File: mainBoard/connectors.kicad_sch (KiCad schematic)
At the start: 55 parts, among them J10 Conn_01x02, J11 Conn_02x05_Odd_Even, J12 Conn_01x02, J14 Conn_01x06, J17 Conn_01x05, J18 Conn_01x04, J19 Conn_01x14, J8 Conn_01x02, J9 Conn_01x02, Q3 IRLML6244TRPBF, Q4 IRLML6244TRPBF, Q5 IRLML6244TRPBF, Q6 IRLML6244TRPBF, Q8 PMOS, U17 SFH617A-2, U18 USBLC6-4SC6, U21 USBLC6-4SC6, U23 USBLC6-4SC6, U24 USBLC6-2SC6, U26 100, U27 100, U28 100, U29 100, U30 74LVC1T45W6-7, U32 74LVC1T45W6-7

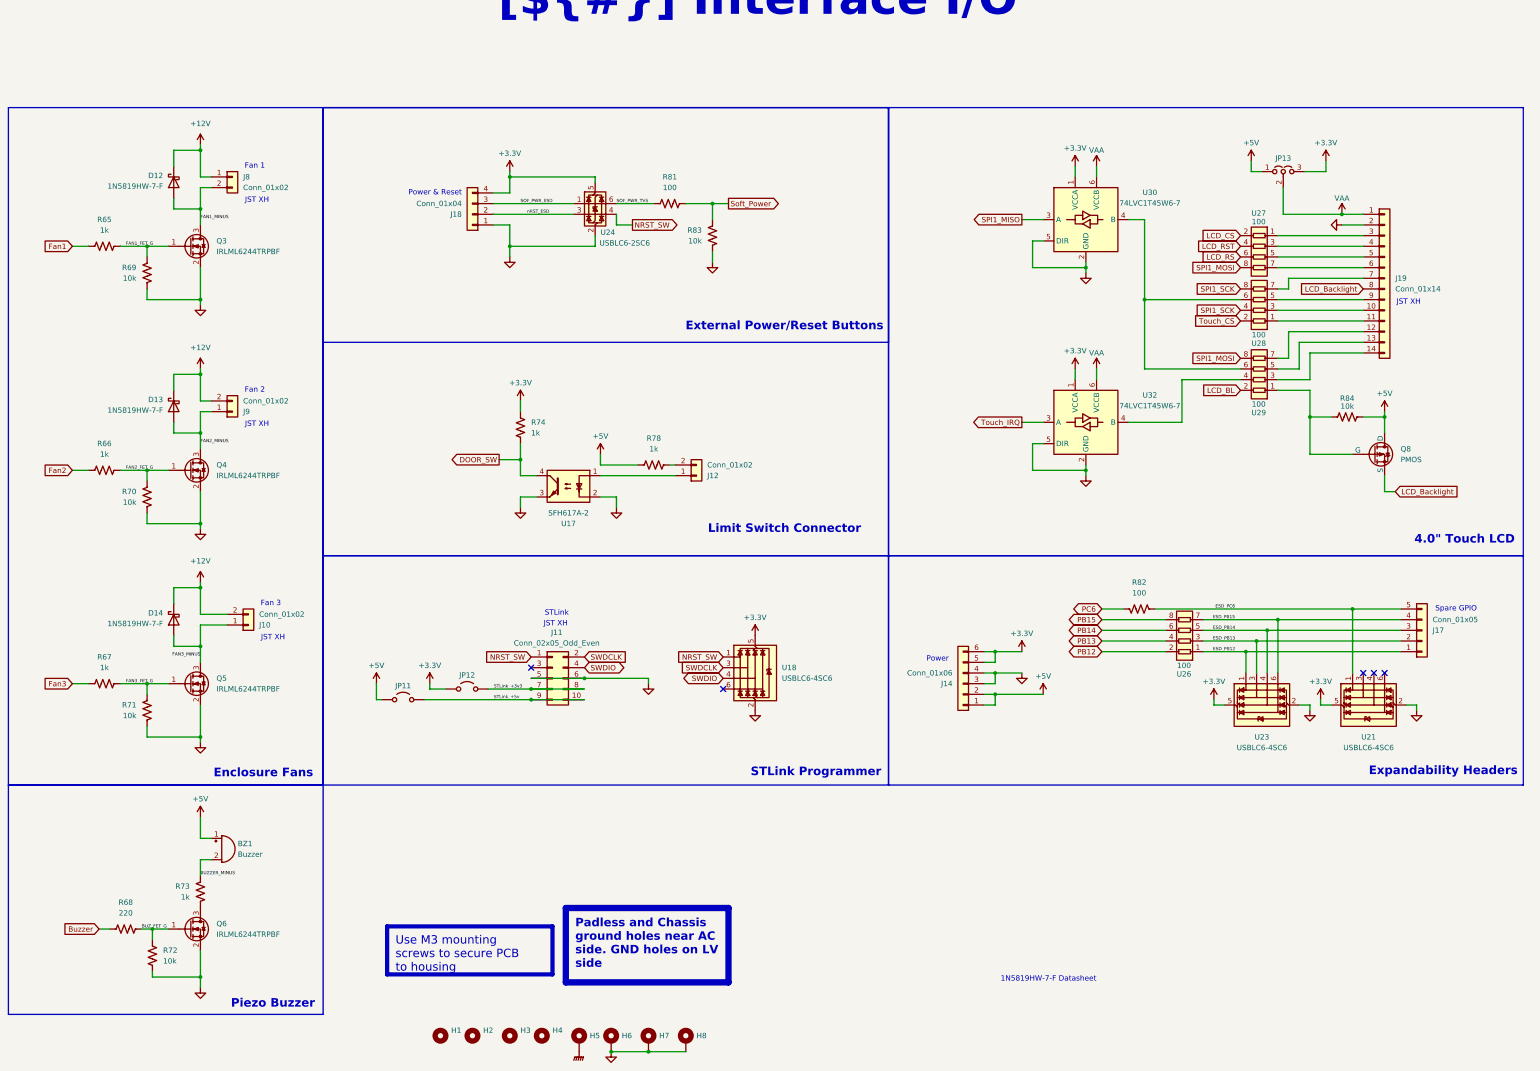
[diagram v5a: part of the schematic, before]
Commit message: replace piezo with actual speaker
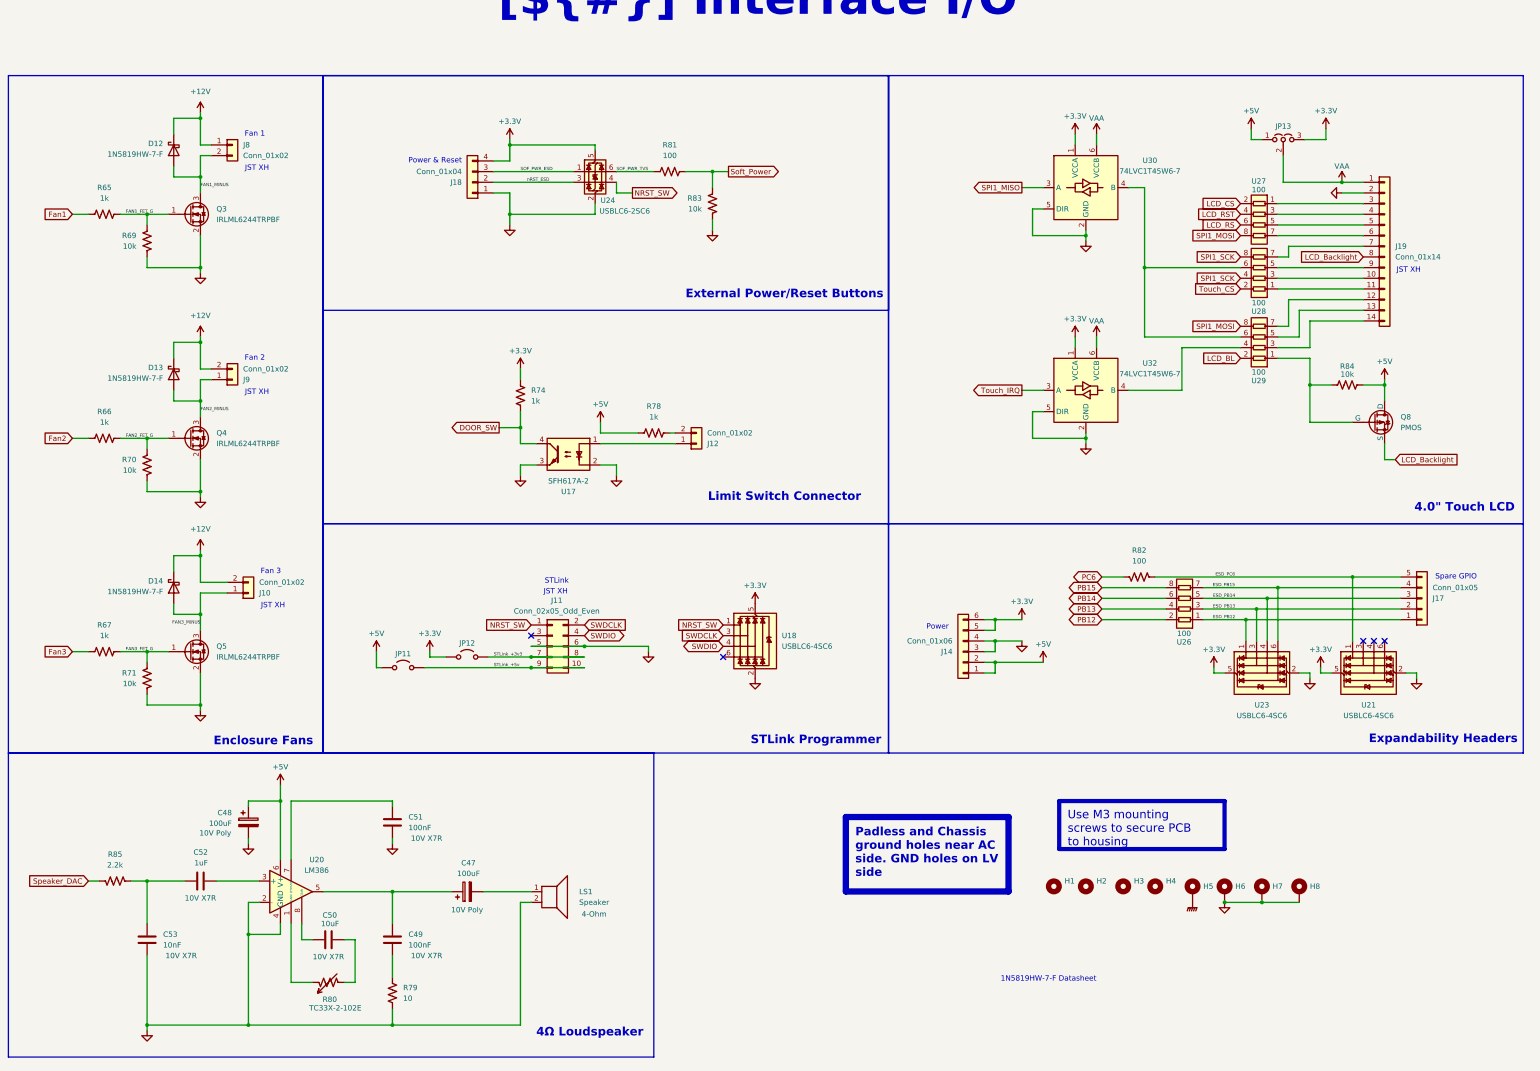
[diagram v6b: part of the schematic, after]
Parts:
- removed BZ1: Buzzer, Buzzer_Beeper:Buzzer_12x9.5RM7.6, symbol Device:Buzzer
- removed Q6: IRLML6244TRPBF, Package_TO_SOT_SMD:SOT-23, symbol Transistor_FET:IRLML6244
- removed R68: 220, Resistor_SMD:R_0603_1608Metric_Pad0.98x0.95mm_HandSolder, symbol Device:R_US
- removed R72: 10k, Resistor_SMD:R_0603_1608Metric_Pad0.98x0.95mm_HandSolder, symbol Device:R_US
- removed R73: 1k, Resistor_SMD:R_0603_1608Metric_Pad0.98x0.95mm_HandSolder, symbol Device:R_US
- added C47, C48: 100uF, Capacitor_SMD:C_Elec_6.3x5.8, symbol Device:C_Polarized
- added C49, C51: 100nF, Capacitor_SMD:C_0805_2012Metric_Pad1.18x1.45mm_HandSolder, symbol Device:C
- added C50: 10uF, Capacitor_SMD:C_0805_2012Metric_Pad1.18x1.45mm_HandSolder, symbol Device:C
- added C52: 1uF, Capacitor_SMD:C_0805_2012Metric_Pad1.18x1.45mm_HandSolder, symbol Device:C
- added C53: 10nF, Capacitor_SMD:C_0603_1608Metric_Pad1.08x0.95mm_HandSolder, symbol Device:C
- added LS1: Speaker, Connector_JST:JST_PH_B2B-PH-K_1x02_P2.00mm_Vertical, symbol Device:Speaker
- added R79: 10, Resistor_SMD:R_0603_1608Metric_Pad0.98x0.95mm_HandSolder, symbol Device:R_US
- added R80: TC33X-2-102E, Potentiometer_SMD:Potentiometer_Bourns_TC33X_Vertical, symbol Device:R_Variable_US
- added R85: 2.2k, Resistor_SMD:R_0603_1608Metric_Pad0.98x0.95mm_HandSolder, symbol Device:R_US
- added U20: LM386, Package_SO:SOIC-8_3.9x4.9mm_P1.27mm, symbol Amplifier_Audio:LM386
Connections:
- net +5V: now also C48.1, U20.6 (V+)
- net GND: now also C48.2, C51.2, C53.2, LS1.2, R79.2, U20.2 (-), U20.4 (GND)
- new net: R80.1, U20.1 (GAIN)
- new net: C50.2, R80.2
- new net: C52.2, U20.3 (+)
- new net: C47.1, C49.1, U20.5
- new net: C51.1, U20.7 (BYPASS)
- new net: C50.1, U20.8 (GAIN)
- new net: C52.1, C53.1, R85.1
- new net: C49.2, R79.1
- new net: C47.2, LS1.1
- new net Speaker_DAC: R85.2
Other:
- note added: "4Ω Loudspeaker"
- note removed: "Piezo Buzzer"
- moved on the sheet: D12, D13, D14, H1, H2, H3, H4, H5, H6, H7, H8, J10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
